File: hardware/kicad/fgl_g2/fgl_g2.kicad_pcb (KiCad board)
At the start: 2 copper layers, 74 x 58 mm, 70 parts, among them J1 USB-C (from bank), J10 XIAO socket 8-14, J2 POT 100k lin + SW, J3 LD2410S socket, J4 LD2410S cable, J5 PORT 1, J6 PORT 2, J7 PORT 3, J8 PORT 4, J9 XIAO socket 1-7, Q1 AO3400A, Q2 AO3401A, U2 TPS61500PWPR

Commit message: G2: fix the Oct 24 audit findings; G2 firmware build with string guards
Hardware (schematic, PCB, fab outputs):
- R18 100k -> 2.2k so EN stays low through reset and USB flashing (H1)
- C5 10u 100V X7S 1210, C6 100n 100V (M2)
- R15 120k -> 110k: OVP 27.7 V, switch <= 35.1 V worst case (M3)
- JP1 solder jumper -> 1x3 2.54 mm header with a shunt (L1)
- Q2 soft start: R14 10k + new C16 100n gate-source (L2)
- Silkscreen: exact JP1 currents, pin-1 mark, "SWITCH OFF BEFORE WIRING PORTS"
- BOM tidy: U1 once, shunt line, voltages/tolerances in values;
  upload BOM in jlcpcb/ refreshed and kept in sync by build.sh

Firmware (src/main.c, platformio env seeed_xiao_esp32c3_g2):
- G2 pins, analog dimming, JP1 ceiling read, 5 W cap
- low-current start probe, open/short/window guards with NVS-learned
  window and relearn gesture, 30 s retry
- pot 1.85 V clamp, radar UART pull-ups, task watchdog (G1 M1/L2/L4)

Docs: g2_decisions.md D16 and updated values/tests, audit resolution,
hardware.md setup steps, README status, ERC summary.

Co-Authored-By: Claude Opus 5.5 <noreply@anthropic.com>
Claude-Session: https://claude.ai/code/session_013HVPKWJHmpHbXpMbmhYHhv
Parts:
- added C16: 100n 16V, Capacitor_SMD:C_0402_1005Metric, F.Cu at (158.6, 121.1)
- C11, C12, C14, C15, C3, C8, C9: value 100n -> 100n 50V
- C5: value 10u 50V -> 10u 100V; footprint Capacitor_SMD:C_1206_3216Metric -> Capacitor_SMD:C_1210_3225Metric
- C6: value 100n -> 100n 100V
- C7: value 1u -> 1u 50V
- JP1: value 500mA -> ISEL; footprint Jumper:SolderJumper-3_P1.3mm_Open_RoundedPad1.0x1.5mm -> Connector_PinHeader_2.54mm:PinHeader_1x03_P2.54mm_Vertical
- R10: value 100R -> 100R 1%
- R11, R13, R23, R7: value 100k -> 100k 1%
- R12: value 33R 1W 2512 -> 33R 1% 1W
- R14: value 1k -> 10k 1%
- R15: value 120k 1% -> 110k 1%
- R17, R22, R26, R27, R28, R6: value 1k -> 1k 1%
- R18: value 100k -> 2.2k 1%
- moved JP1 12.4 mm to (122.5, 116.8)
- moved TP3 1.34 mm to (125.6, 118.6)
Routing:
- net /ISEL: track 22.2 -> 39.3 mm, vias 2 -> 3
- net /RS2_B: track 2.04 -> 12.3 mm, vias 0 -> 1
- net GND: track 35.1 -> 33.9 mm, vias 82 -> 81
- net /LED_RTN: track 88.6 -> 87.7 mm
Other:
- board text added: "1"
- board text added: "JP1 shunt 1-2 (right): 488 mA"
- board text added: "JP1 shunt 2-3 (left): 244 mA"
- board text added: "SWITCH OFF BEFORE WIRING PORTS"
- board text removed: "JP1 open: 250mA"
- board text removed: "bridge all 3: 500mA"

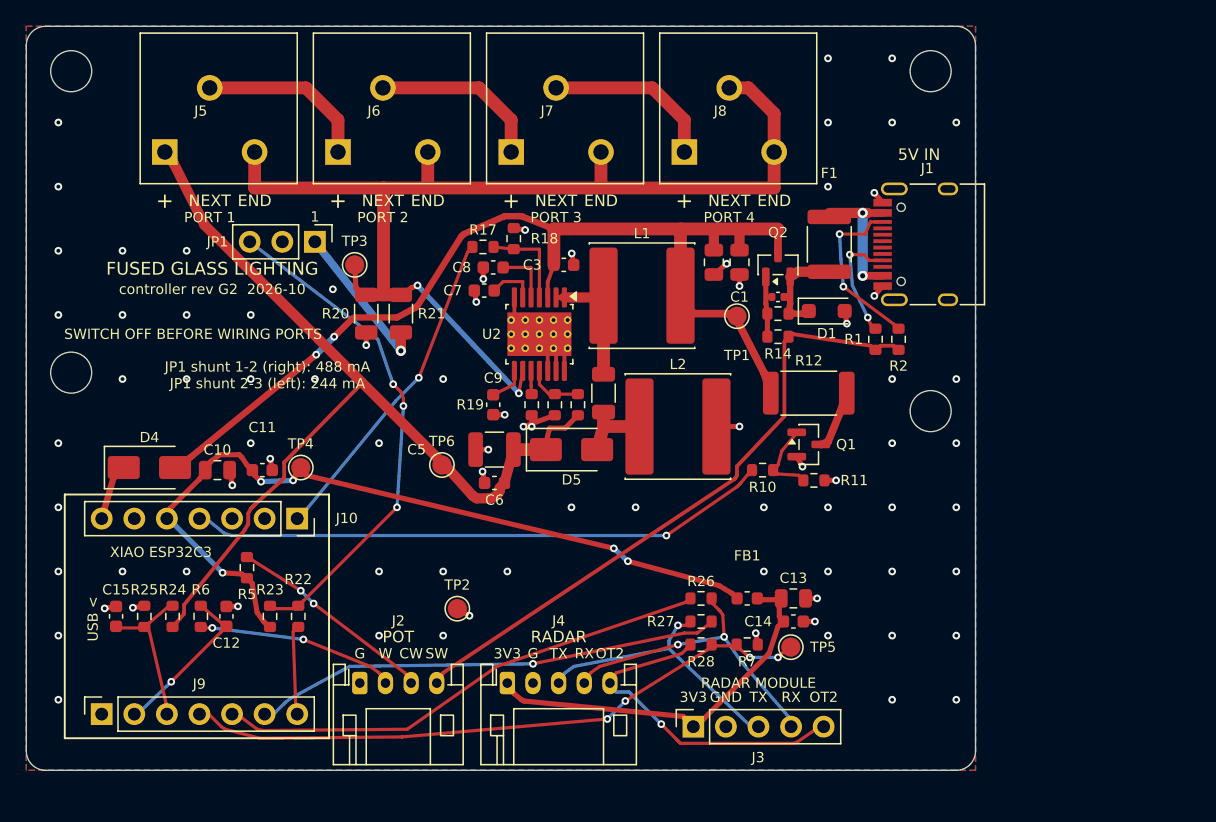
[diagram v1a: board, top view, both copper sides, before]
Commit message: G2 layout DFM pass after Gemini's layout review (D17)
- 25 fan-out vias moved (with their stubs) to >= 0.25 mm from SMD pads:
  C3/C7/C8/R18 from the review, plus a board-wide sweep (incl. a via
  0.06 mm from C5 left by the 1210 change). Three stay closer (no room).
- J3/J4 pin 2 (GND): thermal reliefs instead of solid. J4 spokes at 45;
  J3: RADAR_OT2_C run lowered 1 mm and two GND vias under the socket.
- 10 GND stitching vias between the XIAO and U2.
- F.Fab text tidied; new assembly drawing fgl_g2_assembly.pdf.
- Gerbers/drill regenerated; CPL and position file unchanged.
  DRC 0 errors / 0 unconnected; verify_pcb passes.
- Docs: Gemini's report saved as docs/g2_layout_dfm_audit.md with a
  resolution section; g2_decisions D17, bring-up test G2-T11 (radar vs
  L2), TP5 probe note; 3D render updated.

Co-Authored-By: Claude Opus 5.5 <noreply@anthropic.com>
Claude-Session: https://claude.ai/code/session_013HVPKWJHmpHbXpMbmhYHhv
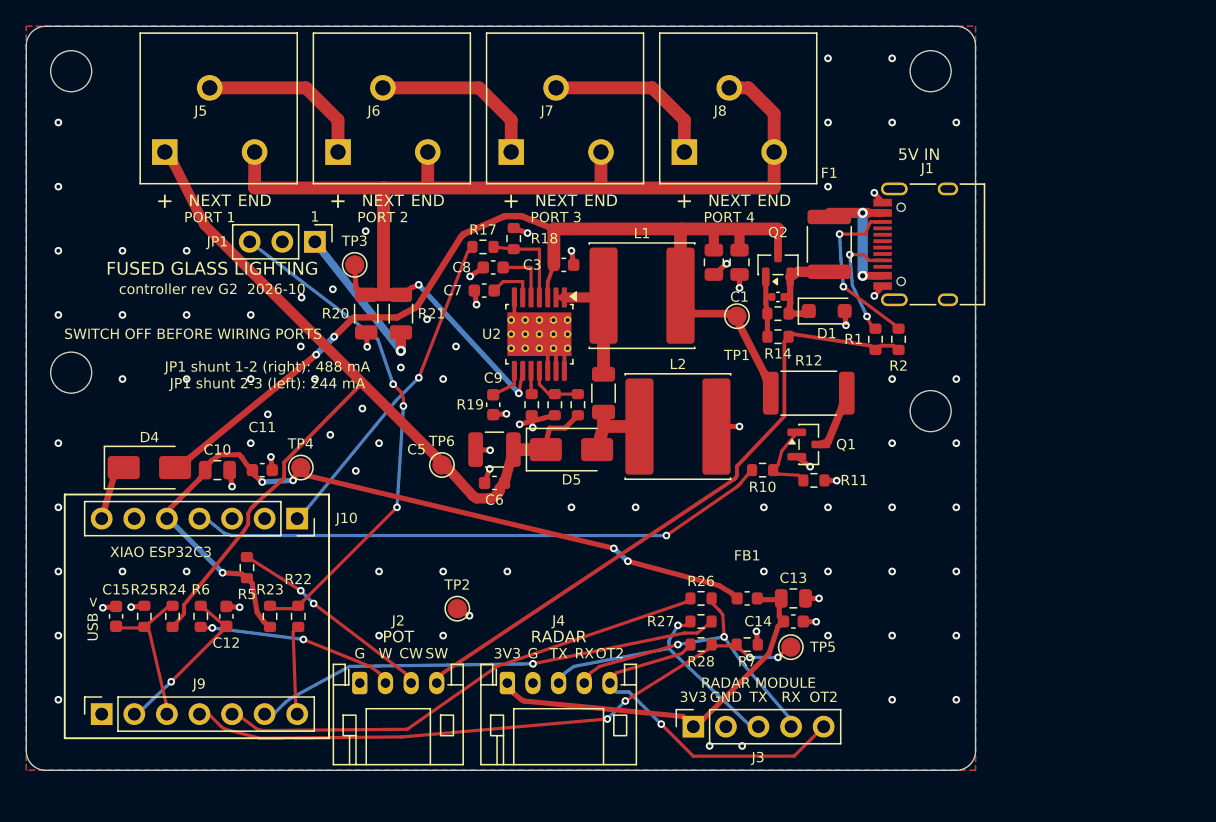
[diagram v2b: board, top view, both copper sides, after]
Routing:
- net GND: track 33.9 -> 37.6 mm, vias 81 -> 93
- net /RADAR_OT2_C: track 26.3 -> 27.3 mm

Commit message: G2: JP2 radar/manual mode jumper (D18)
- JP2 1x3 header (same part as JP1) on XIAO D8/GPIO8: shunt 1-2 = manual
  (radar ignored, lit whenever switched on, pot dims), 2-3 or none = radar.
- No external pull-up (no room by J10): the firmware enables GPIO8's
  internal pull-up and reads the jumper at power-on.
- Layout: JP2 at (114.54, 130), B.Cu route from J10 pin 2, silkscreen
  legend; C11 reference nudged. DRC 0/0, verify_pcb 184 pads.
- Netlist 42 nets / 175 connections / 73 parts; fab outputs, BOM (61
  placements, two loose shunts), assembly drawing, renders regenerated.
- Firmware: manual mode in the G2 build (start check, guards and 5 W cap
  unchanged; no off-delay or radar sleep). Compile-checked with -Werror.
- Docs: D18, pin tables, setup steps, bring-up test G2-T12.

Co-Authored-By: Claude Opus 5.5 <noreply@anthropic.com>
Claude-Session: https://claude.ai/code/session_013HVPKWJHmpHbXpMbmhYHhv
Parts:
- added JP2: RADAR_MODE, Connector_PinHeader_2.54mm:PinHeader_1x03_P2.54mm_Vertical, F.Cu at (114.5, 130.0)
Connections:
- J10 pad 2: (no net) -> /RADAR_MODE
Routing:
- net /RADAR_MODE: track 0.00 -> 11.1 mm
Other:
- board text added: "JP2 1-2 (right): manual"
- board text added: "JP2 2-3 (left): radar"

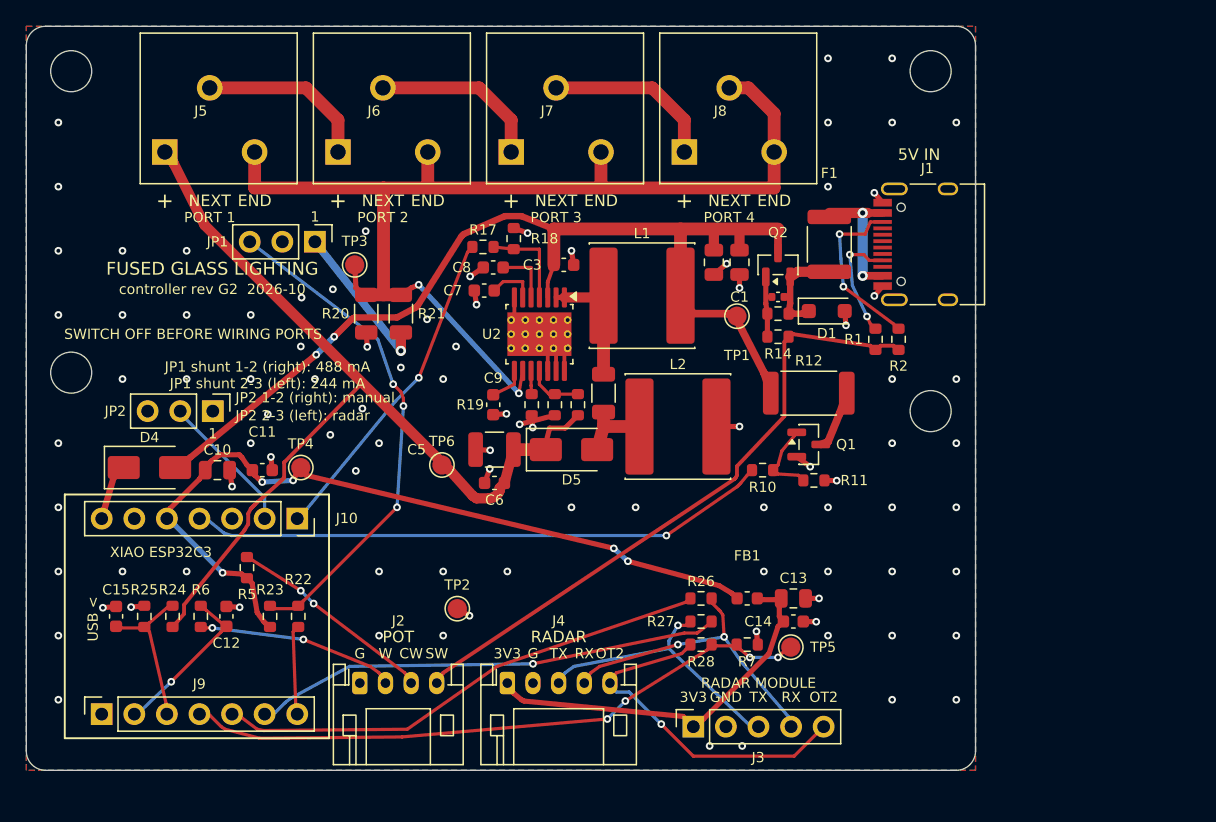
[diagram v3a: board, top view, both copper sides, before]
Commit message: G2: 90 x 60 mm relayout, horizontal-entry ports, R29 pull-up (D19)
- J5-J8: JILN JL212R-35003B01 push-in blocks (Degson DG212R-THR fits the
  same footprint): wire entry parallel to the board at the top edge, release
  buttons on the wire face. New fgl.pretty footprint and a simplified 3D
  model (tools/make_port_step.py).
- R29 10k pull-up on RADAR_MODE (D8); C16 0402 -> 0603 (C14663).
- Board 74 x 58 -> 90 x 60 mm, laid out with tools/layout_g2b: parts spread
  for rework (min courtyard gap 0.72 mm, median ~1 mm, was 0.3 mm), M3 holes
  in the corners, TP5 clear of the radar, FB routed Kelvin to R21, no via
  within 0.25 mm of any SMD pad.
- ERC 0 errors; netlist 42 nets / 177 connections / 74 parts; DRC 0 errors,
  0 unconnected; verify_pcb 186 pads / 69 footprints. Gerbers, drill, CPL
  (62 placements), BOM, assembly drawing, layout image, 3D render regenerated.
- Firmware comment updated for R29; compile-checked with -Werror.
- Docs: D19, pin tables, ordering, bring-up test G2-T13.

Co-Authored-By: Claude Opus 5.5 <noreply@anthropic.com>
Claude-Session: https://claude.ai/code/session_013HVPKWJHmpHbXpMbmhYHhv
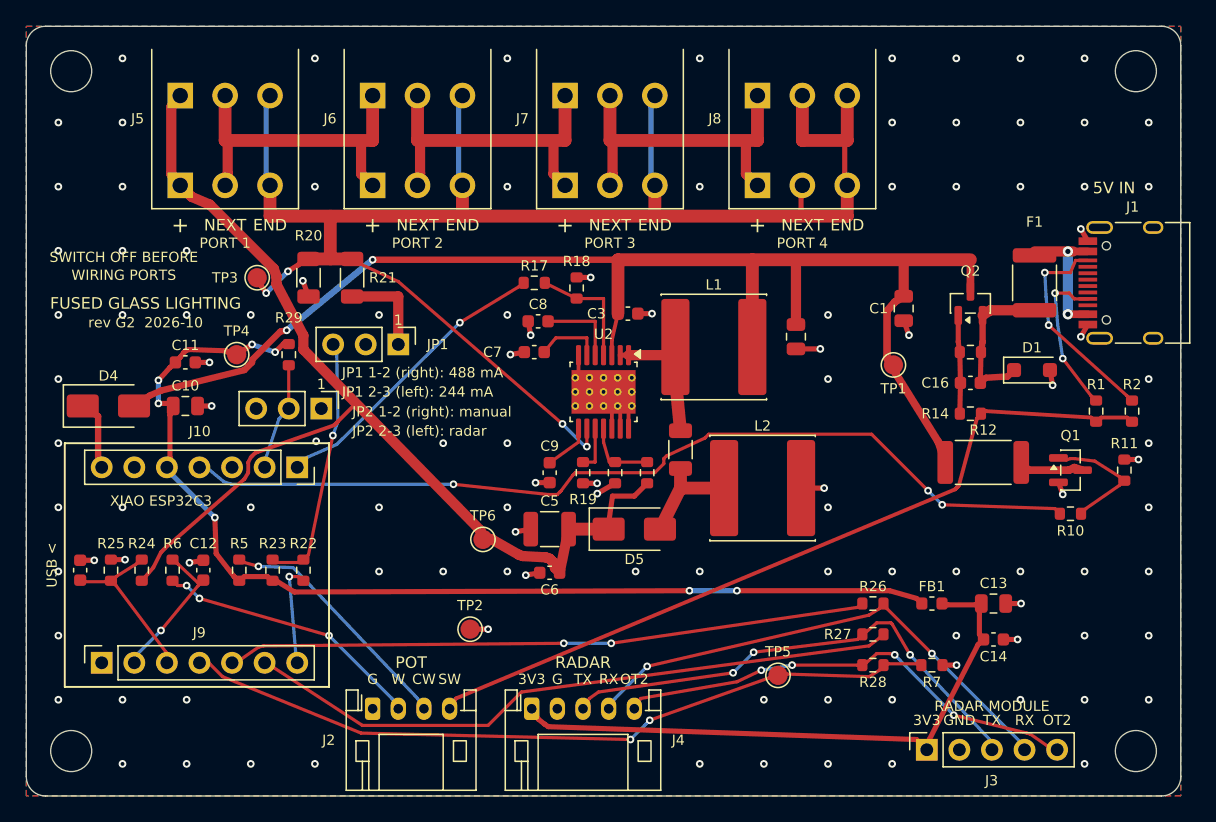
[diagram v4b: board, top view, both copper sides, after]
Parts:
- added R29: 10k, Resistor_SMD:R_0603_1608Metric, F.Cu at (120.5, 125.6)
- C16: value 100n 16V -> 100n 50V; footprint Capacitor_SMD:C_0402_1005Metric -> Capacitor_SMD:C_0603_1608Metric
- J5, J6, J7, J8: footprint fgl:TerminalBlock_Degson_DG250-3.5-03P -> fgl:TerminalBlock_JILN_JL212R-3.5-03P_Horizontal
- moved H4 31.0 mm to (186.5, 156.5)
- moved H3 29.5 mm to (103.5, 156.5)
- moved R10 24.2 mm to (181.4, 138.0)
- moved R11 24.2 mm to (185.6, 134.6), turned to 90 degrees
- moved Q1 20.5 mm to (181.4, 134.6)
- moved R2 19.0 mm to (186.2, 130.0)
- moved J3 18.3 mm to (170.2, 156.4)
- moved R1 18.1 mm to (183.4, 130.0)
- moved D1 16.6 mm to (178.4, 126.8)
- moved C16 16.4 mm to (173.6, 127.8)
- moved F1 16.3 mm to (178.6, 120.0)
- moved J1 16.3 mm to (186.8, 120.0)
- moved R14 16.2 mm to (173.6, 130.2)
- moved H2 16.0 mm to (186.5, 103.5)
- moved C14 15.7 mm to (175.4, 147.8)
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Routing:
- net /LED_RTN: track 87.7 -> 128.6 mm, vias 2 -> 4
- net /KA_DRV: track 45.2 -> 72.0 mm, vias 1 -> 3
- net +5V: track 80.0 -> 106.0 mm
- net +3V3: track 62.9 -> 84.7 mm, vias 5 -> 7
- net /ISEL: track 39.3 -> 19.8 mm, vias 3 -> 1
- net /RADAR_3V3: track 30.4 -> 47.5 mm
- net /RADAR_TX: track 21.8 -> 38.7 mm, vias 1 -> 3
- net /RADAR_RX: track 23.9 -> 39.6 mm
- net /UART_RX: track 36.5 -> 51.3 mm, vias 1 -> 0
- net /VOUT: track 73.2 -> 86.0 mm
- net /STR2: track 13.5 -> 25.9 mm
- net /STR4: track 13.5 -> 25.9 mm
- net /STR3: track 13.5 -> 25.9 mm
- net /SW_N: track 50.0 -> 61.6 mm
- net /UART_TX: track 38.6 -> 49.8 mm, vias 0 -> 2
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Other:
- board size 74 x 58 mm -> 90 x 60 mm
- board text added: "JP1 1-2 (right): 488 mA"
- board text added: "JP1 2-3 (left): 244 mA"
- board text added: "SWITCH OFF BEFORE"
- board text added: "WIRING PORTS"
- board text added: "rev G2 2026-10"
- board text removed: "JP1 shunt 1-2 (right): 488 mA"
- board text removed: "JP1 shunt 2-3 (left): 244 mA"
- board text removed: "SWITCH OFF BEFORE WIRING PORTS"
- board text removed: "controller rev G2 2026-10"
